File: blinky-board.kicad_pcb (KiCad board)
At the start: 2 copper layers, 64.2 x 50.9 mm, 19 parts, among them J1 Conn_01x02_Socket, U1 NE555P, U2 4017

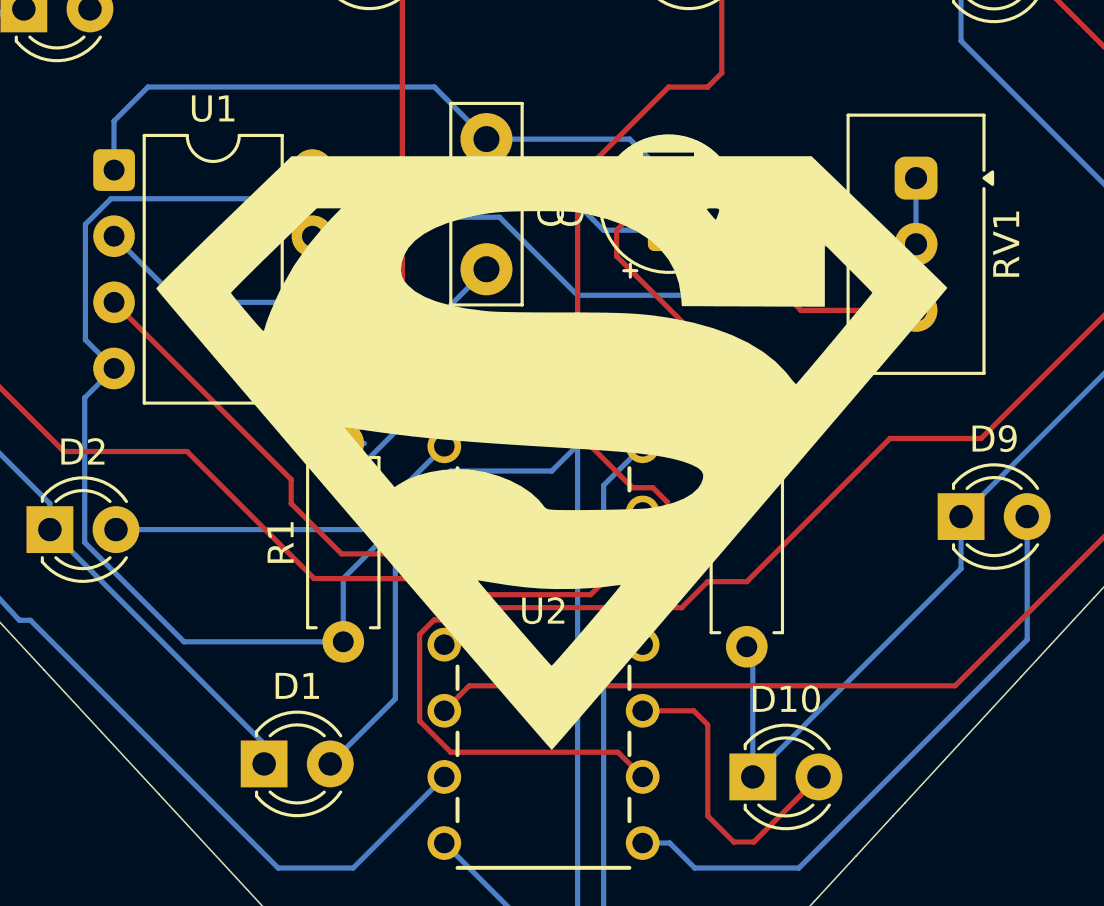
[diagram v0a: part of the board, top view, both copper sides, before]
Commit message: Updated PCB F.Silkscreen
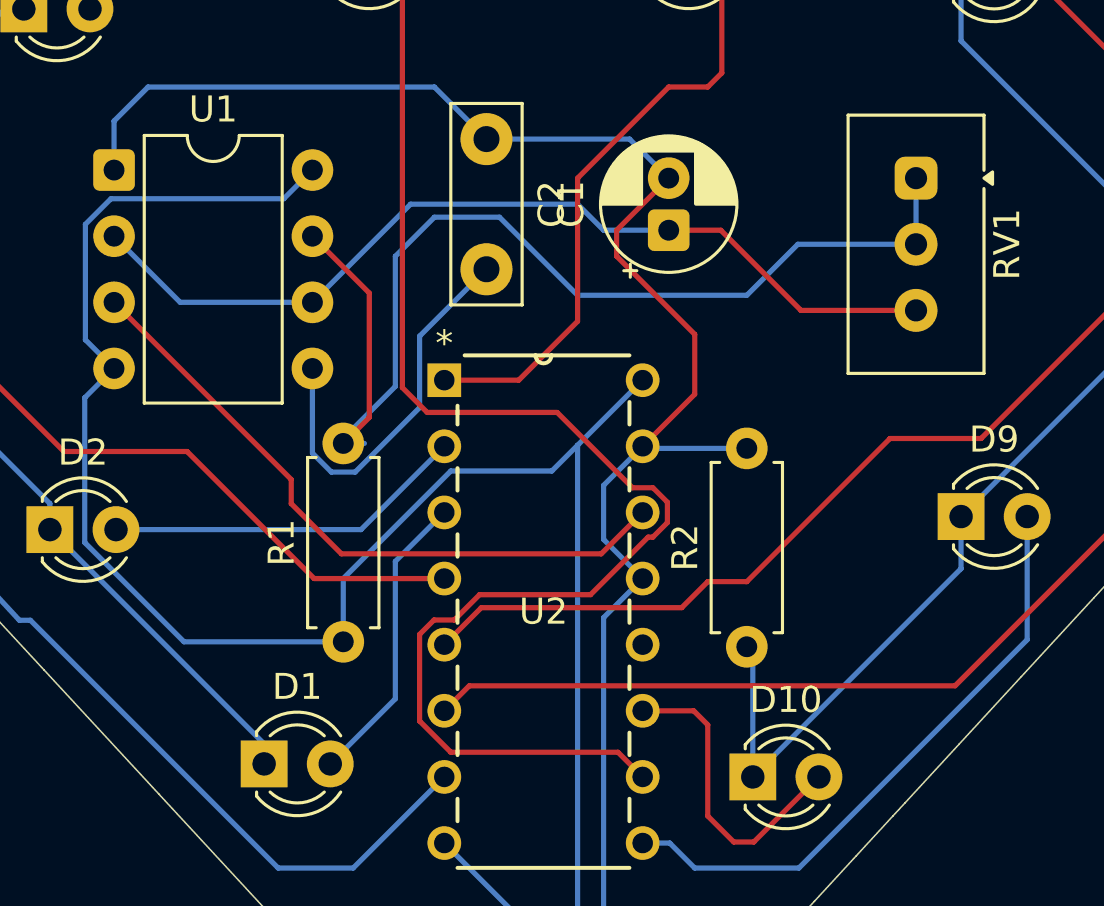
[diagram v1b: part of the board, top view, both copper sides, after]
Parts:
- removed G***: LOGO, Logo:superman_c
